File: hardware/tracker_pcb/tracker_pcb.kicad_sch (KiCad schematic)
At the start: 11 parts, among them J1 256-406, J2 JL308-25409G01, U2 ESP32C6_SEEED, X1 256-402

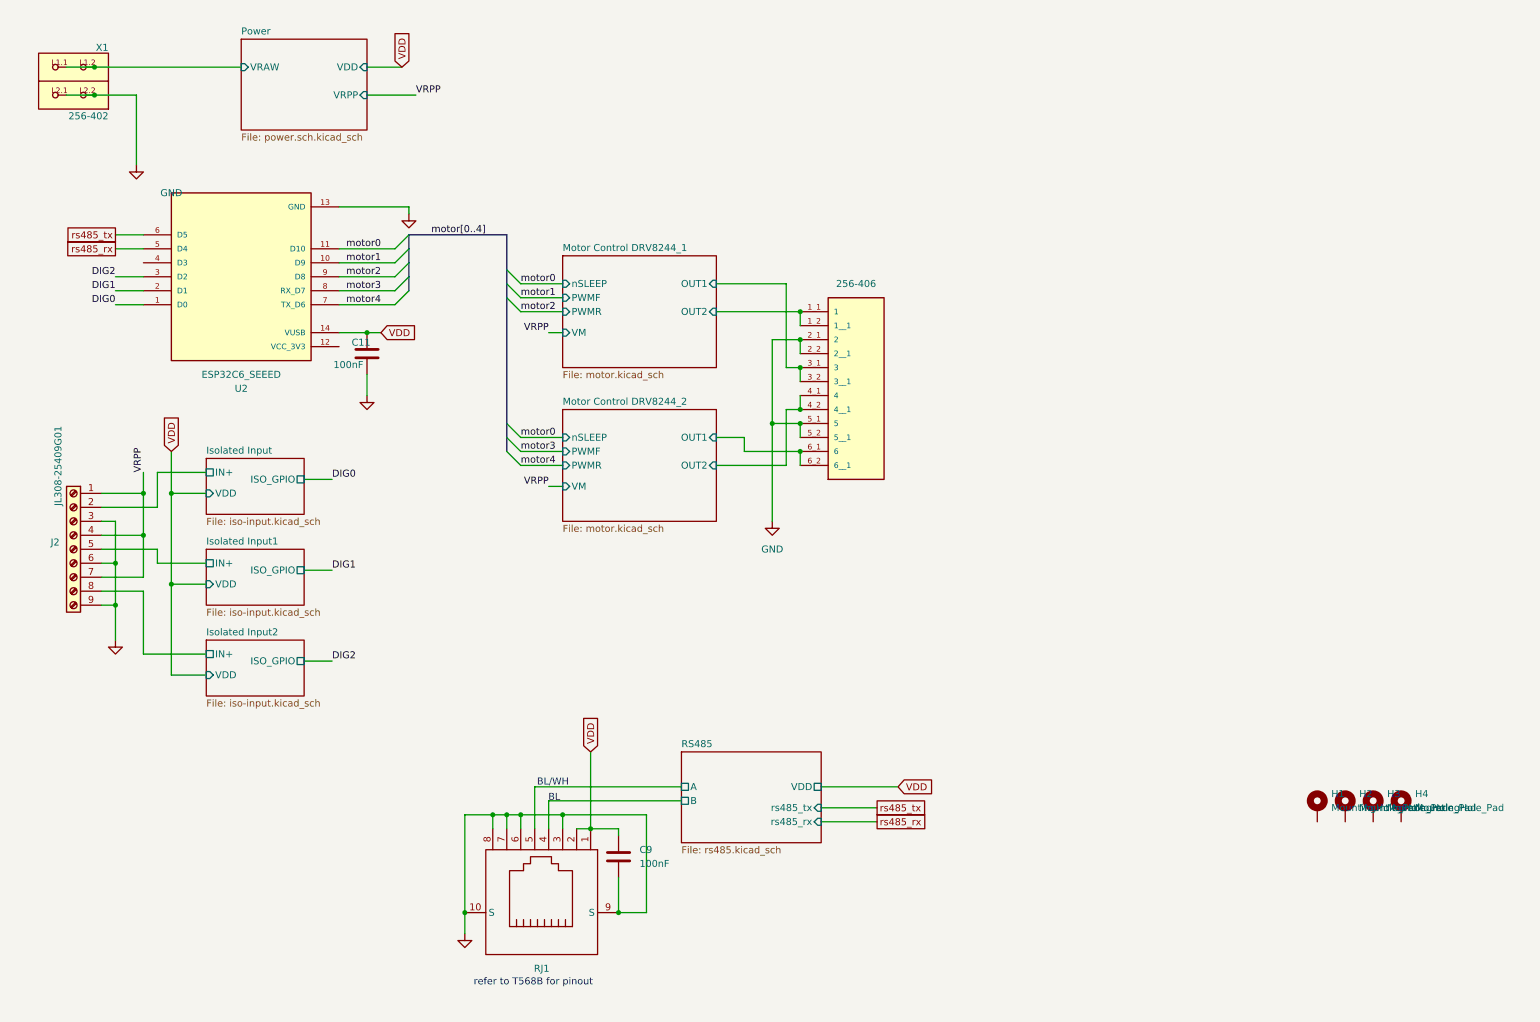
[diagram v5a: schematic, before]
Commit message: Complete but optos are using 5v pullups instead of 3v3.  No bueno
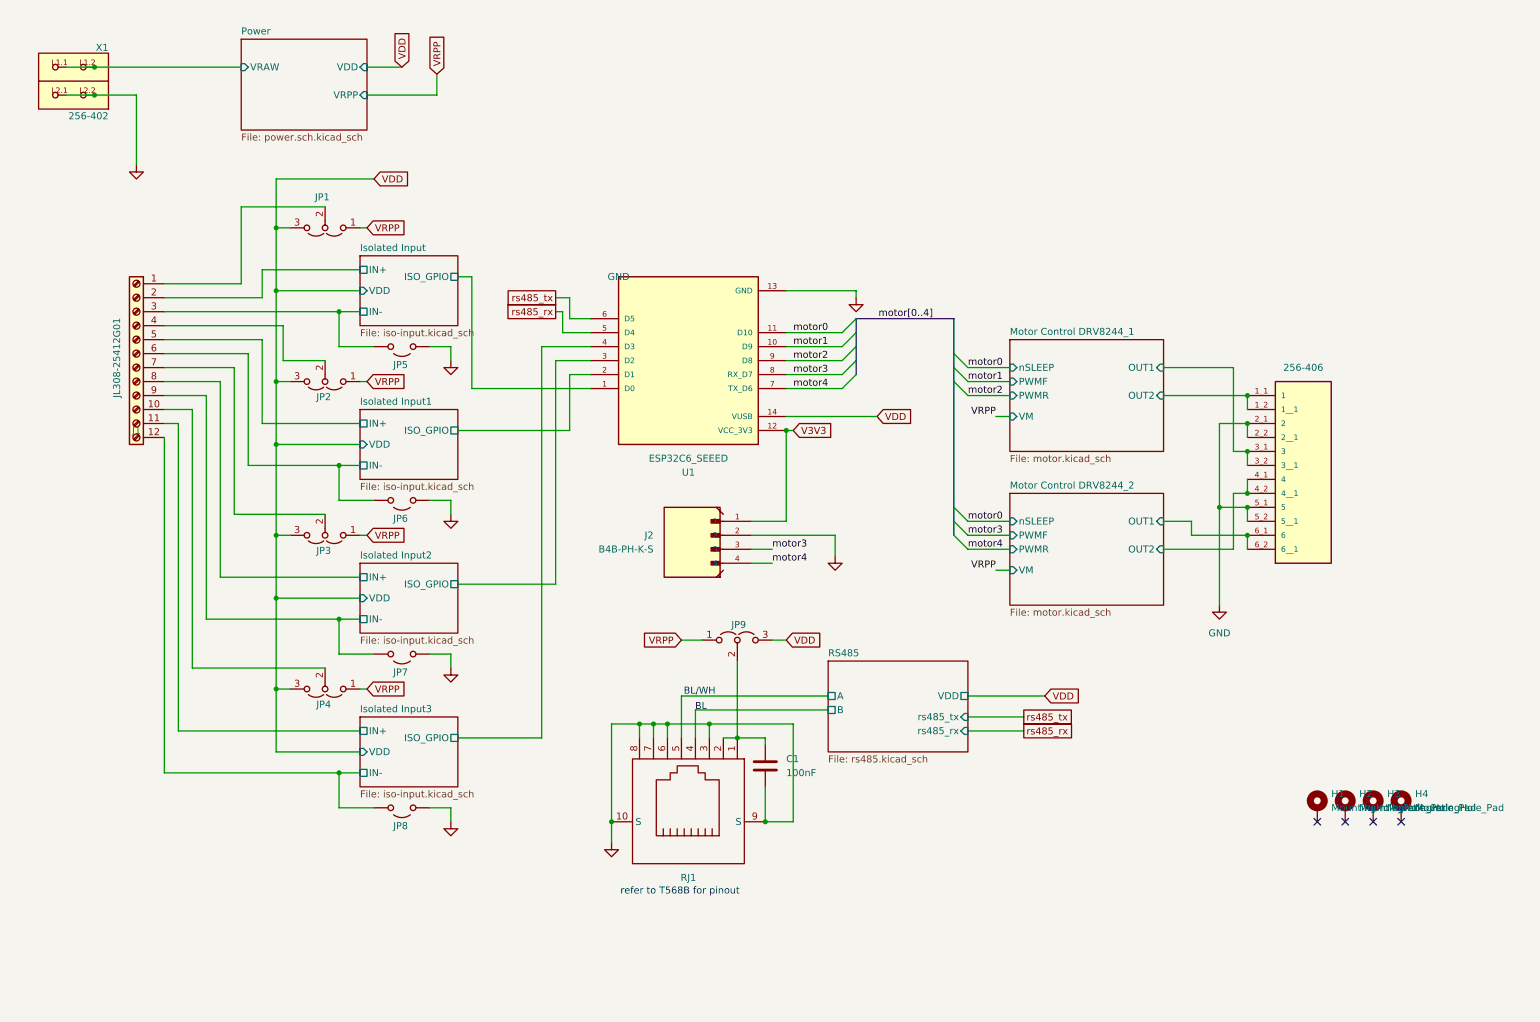
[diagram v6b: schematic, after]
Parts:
- removed C11: 100nF, Capacitor_SMD:C_0603_1608Metric, symbol Device:C
- removed J2: JL308-25409G01, TerminalBlock_TE-Connectivity:TerminalBlock_TE_282834-9_1x09_P2.54mm_Horizontal, symbol Connector:Screw_Terminal_01x09
- added J1: JL308-25412G01, footprint:TE_1-282834-2, symbol Connector:Screw_Terminal_01x12
- added J2: B4B-PH-K-S, footprint:JST_B4B-PH-K-S, symbol symbol:B4B-PH-K-S
- added JP1, JP2, JP3, JP4, JP9: Jumper_3_Open, Connector_PinHeader_2.00mm:PinHeader_1x03_P2.00mm_Vertical, symbol Jumper:Jumper_3_Open
- added JP5, JP6, JP7, JP8: Jumper_2_Open, Connector_PinHeader_2.00mm:PinHeader_1x02_P2.00mm_Vertical, symbol Jumper:Jumper_2_Open
- renumbered C9 to C1, J1 to J3, U2 to U1
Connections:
- net GND: now also J2.2, JP5.1 (A), JP6.1 (A), JP7.1 (A), JP8.1 (A)
- net Isolated Input/IN+: now also J1.2 (Pin_2)
- net Isolated Input1/IN+: now also J1.5 (Pin_5)
- net Isolated Input2/IN+: now also J1.8 (Pin_8)
- net VDD: now also JP1.3 (B), JP2.3 (B), JP3.3 (B), JP4.3 (B), JP9.3 (B); no longer C1.1, RJ1.1, RJ1.2
- net VRPP: now also JP1.1 (A), JP2.1 (A), JP3.1 (A), JP4.1 (A), JP9.1 (A)
- net motor3: now also J2.3
- net motor4: now also J2.4
- net V3V3: now reaches U1.12 (VCC_3V3)
- net V3V3: now also J2.1
- net Isolated Input3/ISO_GPIO: now reaches U1.4 (D3)
- net DIG0 renamed Isolated Input/ISO_GPIO
- net DIG1 renamed Isolated Input1/ISO_GPIO
- net DIG2 renamed Isolated Input2/ISO_GPIO
- new net: J1.10 (Pin_10), JP4.2 (C)
- new net: J1.7 (Pin_7), JP3.2 (C)
- new net: J1.1 (Pin_1), JP1.2 (C)
- new net: J1.4 (Pin_4), JP2.2 (C)
- new net: C1.1, JP9.2 (C), RJ1.1, RJ1.2
- new net Isolated Input/IN-: J1.3 (Pin_3), JP5.2 (B)
- new net Isolated Input1/IN-: J1.6 (Pin_6), JP6.2 (B)
- new net Isolated Input2/IN-: J1.9 (Pin_9), JP7.2 (B)
- new net Isolated Input3/IN+: J1.11 (Pin_11)
- new net Isolated Input3/IN-: J1.12 (Pin_12), JP8.2 (B)
- no-connect marks 0 -> 4
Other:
- added sheet Isolated Input3 (iso-input.kicad_sch)
- sheet Isolated Input ports: added IN-; removed none
- sheet Isolated Input1 ports: added IN-; removed none
- sheet Isolated Input2 ports: added IN-; removed none
- moved on the sheet: C1, RJ1, U1

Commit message: WIP
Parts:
- added D8: SBR2U30P1-7, Diode_SMD:D_PowerDI-123, symbol PCM_JLCPCB-Diodes:Schottky,SS54
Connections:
- net VDD: now also D8.2; no longer U1.14 (VUSB)
- new net: D8.1, U1.14 (VUSB)
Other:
- sheet Isolated Input ports: added 3V3; removed VDD
- sheet Isolated Input1 ports: added 3V3; removed VDD
- sheet Isolated Input2 ports: added 3V3; removed VDD
- sheet Isolated Input3 ports: added 3V3; removed VDD
- company: (none) -> WadeCo Electronics
- title: (none) -> MOtor2ISOlatedInput4

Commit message: Including LORA wio-sx1262
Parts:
- removed C1: 100nF, Capacitor_SMD:C_0603_1608Metric, symbol Device:C
- removed D8: SBR2U30P1-7, Diode_SMD:D_PowerDI-123, symbol PCM_JLCPCB-Diodes:Schottky,SS54
- removed J2: B4B-PH-K-S, footprint:JST_B4B-PH-K-S, symbol symbol:B4B-PH-K-S
- removed RJ1: RJ45 Shielded, footprint:RJ45-TH_R-RJ45S08P-B000, symbol symbol:R-RJ45R08P-B000
- removed U1: ESP32C6_SEEED, footprint:MODULE_113991054, symbol symbol:ESP32C6_SEEED
- added J2: B6B-PH-K-S, footprint:JST_B6B-PH-K-S, symbol symbol:B6B-PH-K-S
- added J5: B4B-XH-A, footprint:JST_B4B-XH-A, symbol symbol:B4B-XH-A
- added JP10: Jumper_3_Open, Connector_PinHeader_2.00mm:PinHeader_1x03_P2.00mm_Vertical, symbol Jumper:Jumper_3_Open
- J1: LCSC (none) -> C2922607
- J3: LCSC (none) -> C3309533
- JP1, JP2, JP3, JP4, JP9: LCSC (none) -> C265013
- JP5, JP6, JP7, JP8: LCSC (none) -> C160332
- X1: LCSC (none) -> C2978143
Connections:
- net GND: now also J2.6, J5.4
- net RS485/A: now also J5.2
- net RS485/B: now also J5.3
- net VDD: now also JP10.1 (A)
- net at JP9.2 (C): now also J5.1
- new net: J2.1, JP10.2 (C)
- new net IO21: J2.2
- new net IO22: J2.3
- new net IO23: J2.4
- new net NSS_CS3: J2.5
- new net V33: JP10.3 (B)
- no-connect marks 4 -> 6
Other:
- added sheet LORA (lora.kicad_sch)
- added sheet esp32 (esp32.kicad_sch)
- sheet Motor Control DRV8244_1 ports: added IOUT, SCLK, SDI, SDO, nSCS; removed nSLEEP
- sheet Motor Control DRV8244_2 ports: added IOUT, SCLK, SDI, SDO, nSCS; removed nSLEEP
- sheet Power ports: added V33, VBUS; removed none
- sheet RS485 ports: added V33; removed VDD
- note added: "SPI CHIP SELECTS"
- note removed: "BL"
- note removed: "BL/WH"
- note removed: "refer to T568B for pinout"
- moved on the sheet: JP9
